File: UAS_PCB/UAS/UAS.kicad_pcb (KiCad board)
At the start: 2 copper layers, 50.8 x 47.6 mm, 17 parts, among them J1 SM02B-PASS-TBT, J2 SM02B-PASS-TBT, J3 SM02B-PASS-TBT, J4 SM02B-PASS-TBT, U1 JST-7-Pin, U10 UAS-rescue_7.5V-2.4A-Converte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, U11 JST-3-Pin, U12 Signal-Pad, U13 Signal-Pad, U2 5A-5V-Converter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

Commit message: slight adjustments to footprint placement
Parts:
- moved U9 0.32 mm to (159.0, 121.0)
- moved U10 0.10 mm to (155.4, 111.8)
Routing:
- net +7.5V: track 40.3 -> 38.6 mm
- net Net-(U13-Pad1): track 37.5 -> 36.9 mm
- net (no net): vias 0 -> 4
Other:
- outline, holes or cut-outs redrawn
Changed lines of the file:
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@@
   (general
     (thickness 1.6002)
-    (drawings 15227)
-    (tracks 197)
+    (drawings 15223)
+    (tracks 196)
     (zones 0)
     (modules 17)
@@
   )
   (setup
-    (last_trace_width 0.127)
+    (last_trace_width 0.6)
     (user_trace_width 0.15)
     (user_trace_width 0.2)
@@
     (user_via 0.9 0.4)
     (user_via 1.1 0.5)
+    (user_via 2.5 2)
     (uvia_size 0.6858)
     (uvia_drill 0.3302)
@@
   )
   (module UAS:Pololu_7.75V_2.4A_Step_Down_Regulator (layer Front)
-    (at 155.5 111.75 270)
+    (at 155.4 111.75 270)
     (fp_text reference U10 (at 0 4.25 180) (layer F.SilkS)
       (effects (font (size 1 1) (thickness 0.15)))
@@
   )
   (module "UAS:JST_SM03B-PASS-TBT(LF)(SN)" (layer Back)
-    (at 159.3215 121)
+    (at 159 121)
     (fp_text reference U9 (at 0 -3.75) (layer B.SilkS)
       (effects (font (size 1 1) (thickness 0.015)) (justify mirror))
@@
   (gr_line (start 152.542524 92.758045) (end 152.410237 92.542725) (layer B.SilkS) (width 0.0125))
   (gr_line (start 153.5 96) (end 153.514988 95.928529) (layer B.SilkS) (width 0.0125))
-  (gr_circle (center 120 118.545) (end 121 118.545) (layer Edge.Cuts) (width 0.1))
   (gr_line (start 168.26 118.544999) (end 168.26 76) (layer Edge.Cuts) (width 0.1))
   (gr_arc (start 120.000001 76) (end 120 73.46) (angle -90) (layer Edge.Cuts) (width 0.1))
@@
   (gr_line (start 165.72 73.46) (end 120 73.46) (layer Edge.Cuts) (width 0.1))
   (gr_line (start 120.000001 121.084999) (end 165.72 121.084999) (layer Edge.Cuts) (width 0.1))
-  (gr_circle (center 165.72 76) (end 166.72 76) (layer Edge.Cuts) (width 0.1))
-  (gr_circle (center 165.72 118.544999) (end 166.72 118.544999) (layer Edge.Cuts) (width 0.1))
   (gr_arc (start 165.72 118.544999) (end 165.72 121.084999) (angle -90) (layer Edge.Cuts) (width 0.1))
   (gr_line (start 117.460001 76) (end 117.460001 118.545) (layer Edge.Cuts) (width 0.1))
   (gr_arc (start 165.72 76) (end 168.26 76) (angle -90) (layer Edge.Cuts) (width 0.1))
-  (gr_circle (center 120 76) (end 121 76) (layer Edge.Cuts) (width 0.1))
+  (via (at 120 118.55) (size 2.5) (drill 2) (layers Front Back) (net 0) (status 40000))
+  (via (at 120 76) (size 2.5) (drill 2) (layers Front Back) (net 0) (status 40000))
+  (via (at 165.725 76) (size 2.5) (drill 2) (layers Front Back) (net 0) (status 40000))
+  (via (at 165.72 118.54) (size 2.5) (drill 2) (layers Front Back) (net 0) (status 40000))
   (via (at 151.77 99.85) (size 0.9) (drill 0.4) (layers Front Back) (net 1))
   (segment (start 151.77 91.88) (end 151.77 99.85) (width 0.6) (layer Back) (net 1))
@@
   (segment (start 125.25 118.72) (end 125.21 118.76) (width 0.6) (layer Front) (net 27))
   (segment (start 125.25 115.5) (end 125.25 118.72) (width 0.6) (layer Front) (net 27))
-  (segment (start 157.261533 112.009967) (end 157.3215 111.95) (width 0.4) (layer Back) (net 28))
   (via (at 131.3 120.457999) (size 0.9) (drill 0.4) (layers Front Back) (net 28))
   (segment (start 130.207999 120.457999) (end 128.5 118.75) (width 0.6) (layer Front) (net 28))
@@
   (segment (start 152.8 119.507989) (end 151.807989 120.5) (width 0.6) (layer Back) (net 28))
   (segment (start 152.8 118.4) (end 152.8 119.507989) (width 0.6) (layer Back) (net 28))
-  (segment (start 152.8 112.4) (end 153.65 111.7) (width 0.6) (layer Back) (net 28))
-  (segment (start 157.0715 111.7) (end 157.3215 111.95) (width 0.6) (layer Back) (net 28))
-  (segment (start 153.65 111.7) (end 157.0715 111.7) (width 0.6) (layer Back) (net 28))
   (via (at 152.8 118.4) (size 0.9) (drill 0.4) (layers Front Back) (net 28))
   (segment (start 152.8 112.4) (end 152.8 118.4) (width 0.6) (layer Front) (net 28))
   (via (at 152.8 112.4) (size 0.9) (drill 0.4) (layers Front Back) (net 28))
+  (segment (start 153.25 111.95) (end 152.8 112.4) (width 0.6) (layer Back) (net 28))
+  (segment (start 157 111.95) (end 153.25 111.95) (width 0.6) (layer Back) (net 28))
   (via (at 146.7 101.8) (size 1.1) (drill 0.5) (layers Front Back) (net 29))
   (via (at 137.8 74) (size 0.9) (drill 0.4) (layers Front Back) (net 29))
@@
   (segment (start 134.31 101.31) (end 133.5 100.5) (width 1) (layer Back) (net 30))
   (segment (start 143 118) (end 143 114.33) (width 0.6) (layer Front) (net 31))
-  (segment (start 147.88 109.46) (end 147.91 109.43) (width 0.6) (layer Front) (net 31))
   (segment (start 129.23 104.71) (end 129.23 104.08) (width 0.4) (layer Front) (net 31))
   (segment (start 126.5 107.44) (end 129.23 104.71) (width 0.6) (layer Front) (net 31))
@@
   (segment (start 143 110.87) (end 144.66 109.21) (width 0.6) (layer Front) (net 31))
   (segment (start 143 114.33) (end 143 111.12) (width 0.6) (layer Front) (net 31))
-  (segment (start 144.66 109.21) (end 147.88 109.21) (width 0.6) (layer Front) (net 31))
   (via (at 150.25 109.75) (size 0.9) (drill 0.4) (layers Front Back) (net 31))
   (segment (start 149.71 109.21) (end 150.25 109.75) (width 0.6) (layer Front) (net 31))
-  (segment (start 147.88 109.21) (end 149.71 109.21) (width 0.6) (layer Front) (net 31))
   (segment (start 151 109.75) (end 152.21 108.54) (width 0.6) (layer Back) (net 31))
   (segment (start 150.25 109.75) (end 151 109.75) (width 0.6) (layer Back) (net 31))
+  (segment (start 144.66 109.21) (end 147.78 109.21) (width 0.6) (layer Front) (net 31))
+  (segment (start 149.71 109.21) (end 147.78 109.21) (width 0.6) (layer Front) (net 31))
   (segment (start 126.75 111.95) (end 126.75 113.03) (width 0.4) (layer Back) (net 32))
   (segment (start 147.87 114.55) (end 147.88 114.54) (width 0.4) (layer Back) (net 32))
@@
   (segment (start 126.75 112.799962) (end 127.820038 113.87) (width 0.6) (layer Back) (net 32))
   (segment (start 126.75 111.95) (end 126.75 112.799962) (width 0.4) (layer Back) (net 32))
-  (segment (start 159.3215 113.0585) (end 159.3215 111.95) (width 0.4) (layer Back) (net 32))
   (segment (start 147.88 114.54) (end 148.54 113.88) (width 0.4) (layer Back) (net 32))
-  (segment (start 159.3215 112.388602) (end 159.3215 111.95) (width 0.4) (layer Back) (net 32))
   (segment (start 147.88 114.54) (end 148.44 113.98) (width 0.4) (layer Back) (net 32))
-  (segment (start 159.3215 112.9285) (end 159.3215 112.388602) (width 0.6) (layer Back) (net 32))
   (segment (start 132.85 114.29) (end 132.43 113.87) (width 0.6) (layer Back) (net 32))
-  (segment (start 147.88 114.29) (end 132.85 114.29) (width 0.6) (layer Back) (net 32))
   (segment (start 148.27 113.9) (end 147.88 114.29) (width 0.6) (layer Back) (net 32))
-  (segment (start 157.990102 113.9) (end 148.27 113.9) (width 0.6) (layer Back) (net 32))
-  (segment (start 159.3215 112.568602) (end 157.990102 113.9) (width 0.6) (layer Back) (net 32))
-  (segment (start 159.3215 111.95) (end 159.3215 112.568602) (width 0.6) (layer Back) (net 32))
+  (segment (start 132.85 114.29) (end 147.78 114.29) (width 0.6) (layer Back) (net 32))
+  (segment (start 148.17 113.9) (end 147.78 114.29) (width 0.6) (layer Back) (net 32))
+  (segment (start 157.990102 113.9) (end 148.17 113.9) (width 0.6) (layer Back) (net 32))
+  (segment (start 159 112.890102) (end 157.990102 113.9) (width 0.6) (layer Back) (net 32))
+  (segment (start 159 111.95) (end 159 112.890102) (width 0.6) (layer Back) (net 32))
 )

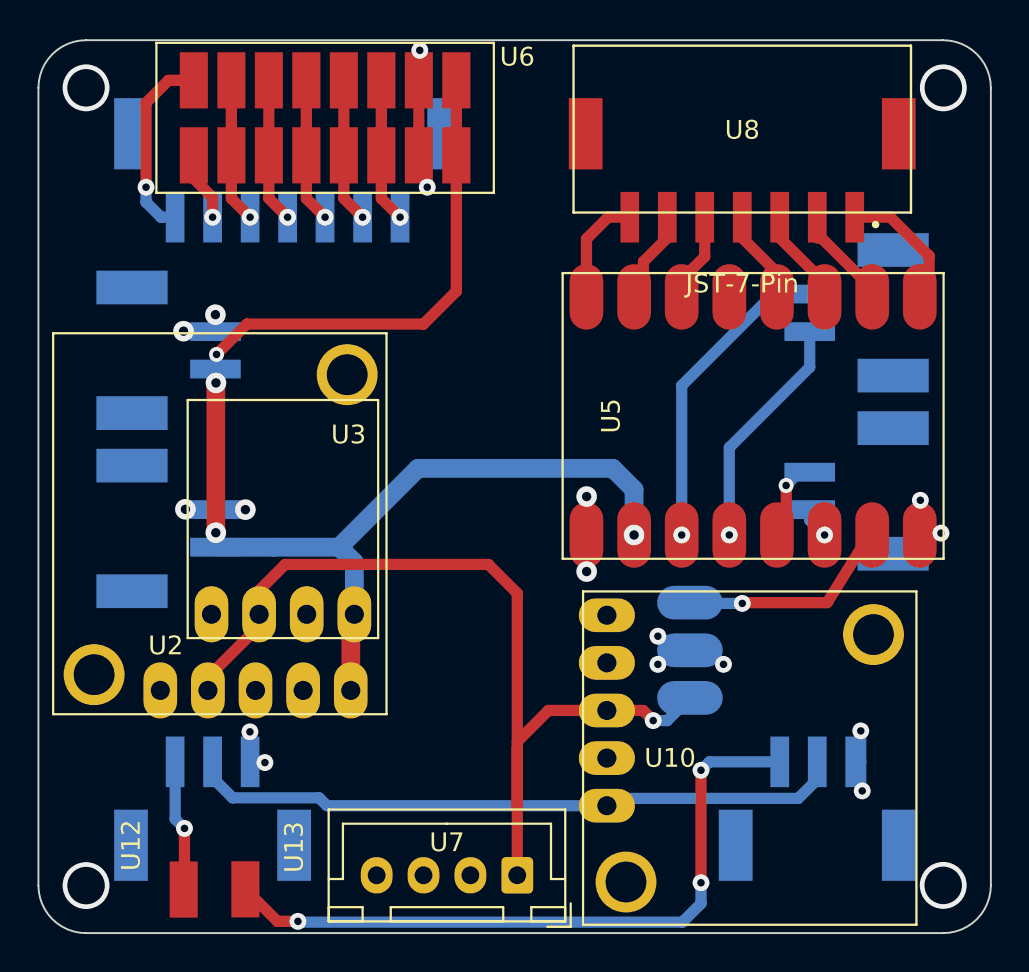
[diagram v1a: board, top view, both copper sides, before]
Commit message: added LeMonke Graphics, still needs trace width adjustments
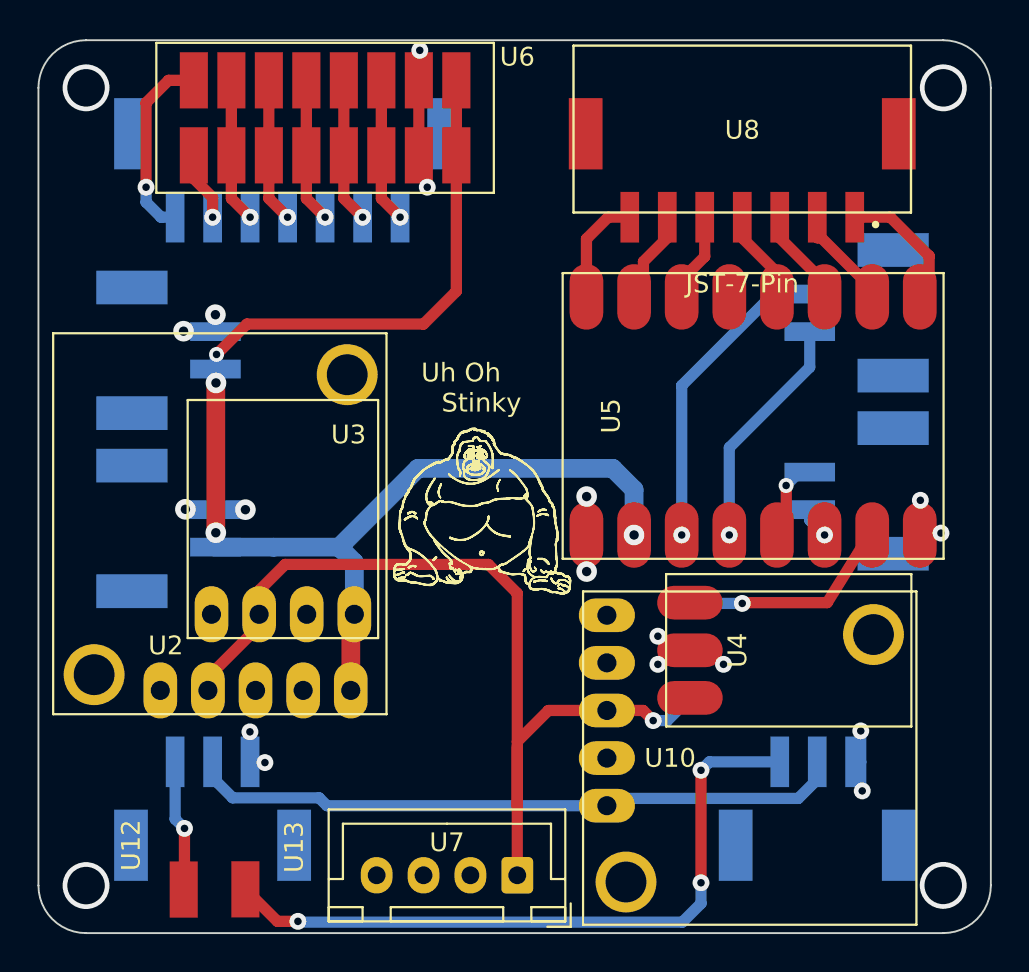
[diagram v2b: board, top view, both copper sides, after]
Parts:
- U4: moved to F.Cu
- turned U4 to 270 degrees
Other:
- board text added: "Uh Oh Stinky"

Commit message: trace width changes
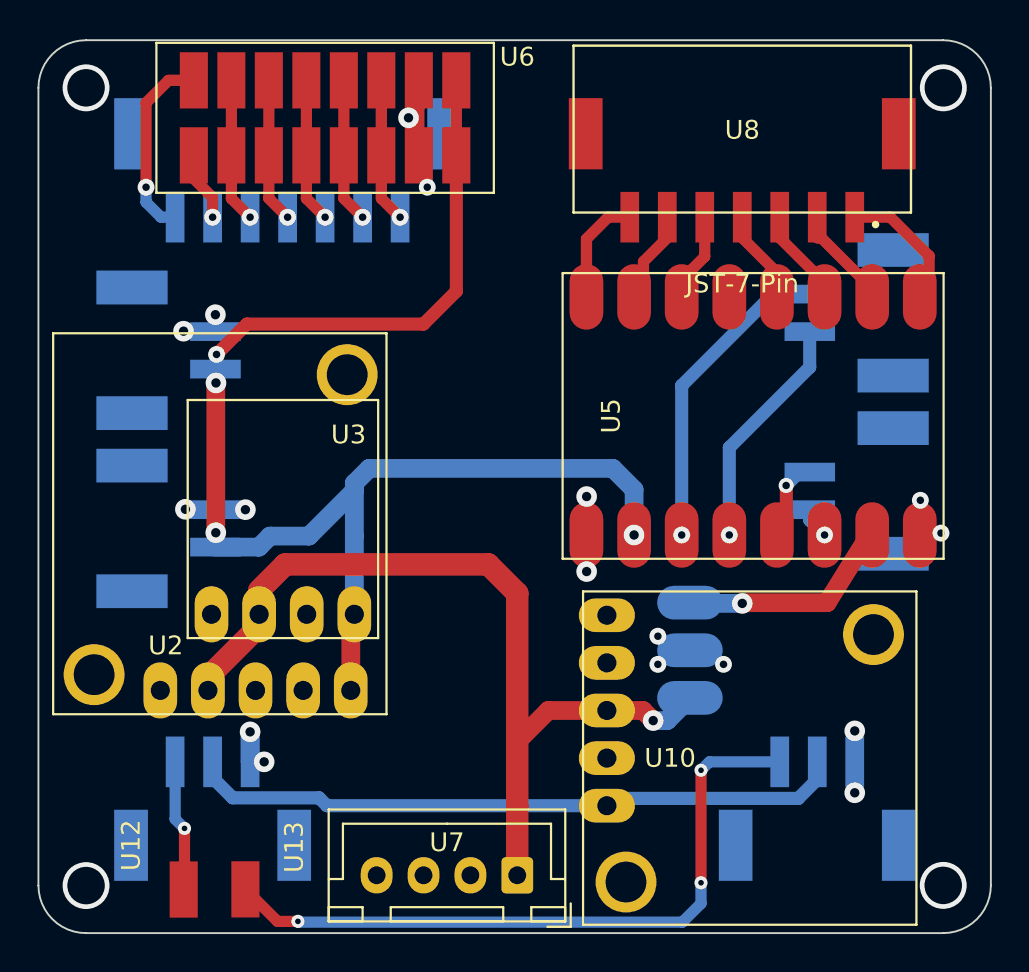
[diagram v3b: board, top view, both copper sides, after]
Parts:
- U4: moved to B.Cu
- turned U4 to 90 degrees
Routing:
- net +5V: track 72.7 -> 76.0 mm
- net GND: track 12.6 -> 14.9 mm

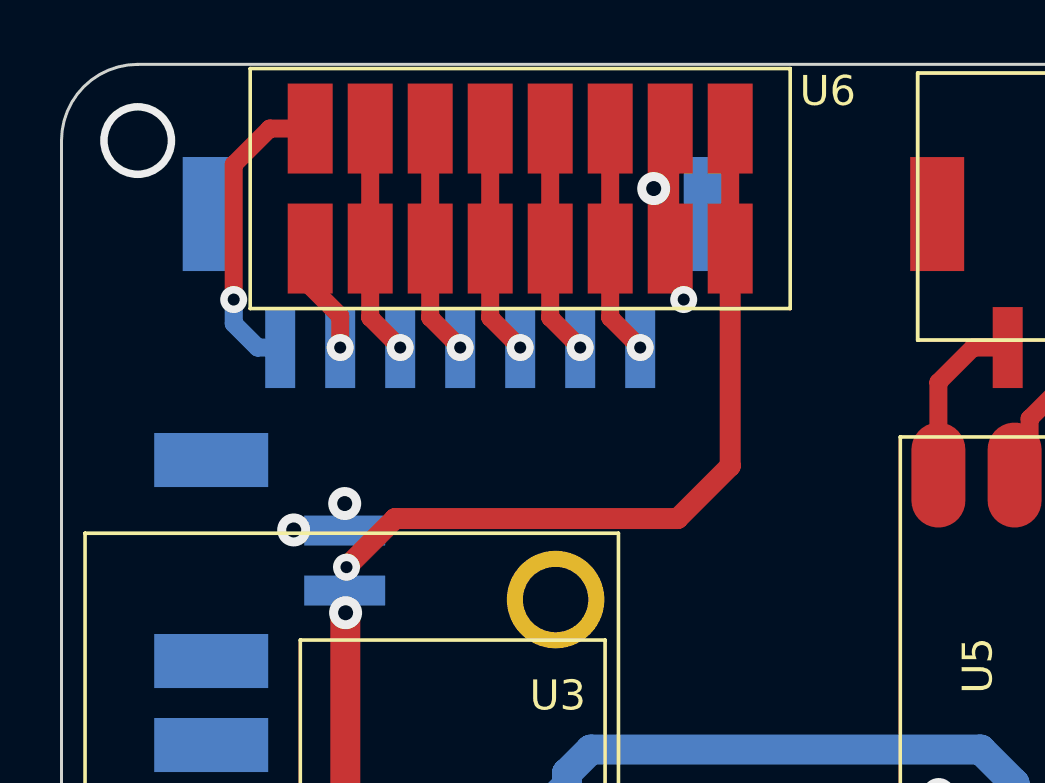
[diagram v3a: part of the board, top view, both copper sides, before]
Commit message: flipped PCS connector to front
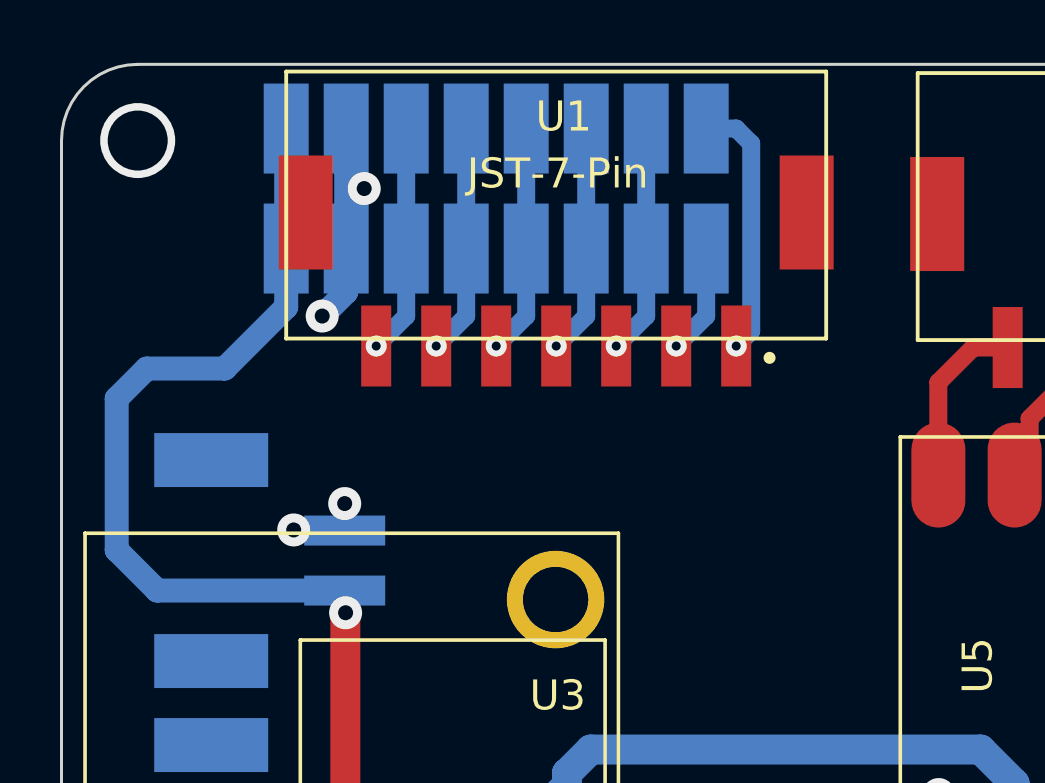
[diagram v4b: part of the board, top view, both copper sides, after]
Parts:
- U1: moved to F.Cu
- U6: moved to B.Cu
- moved U1 3.20 mm to (133.9, 73.7), turned to 0 degrees
- moved U6 0.80 mm to (131.9, 79.6), turned to 180 degrees
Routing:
- net GND: track 14.9 -> 17.5 mm
- net Net-(U1-Pad1): track 10.2 -> 8.66 mm
- net +5V: track 76.0 -> 75.8 mm, vias 4 -> 3

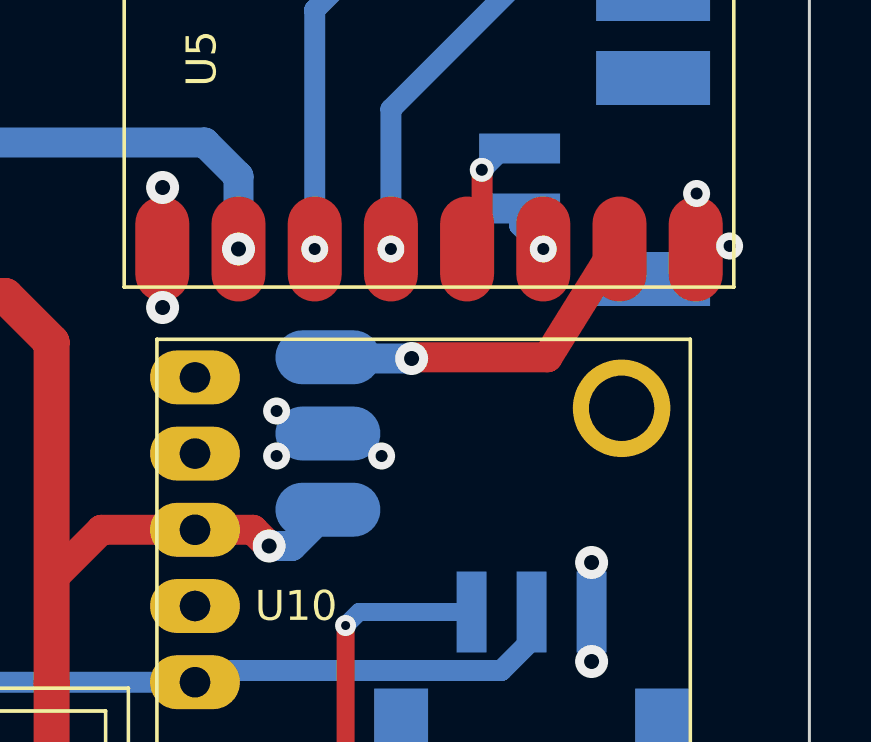
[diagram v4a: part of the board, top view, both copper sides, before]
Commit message: 12v step up was backwards
should double check other pinouts as well
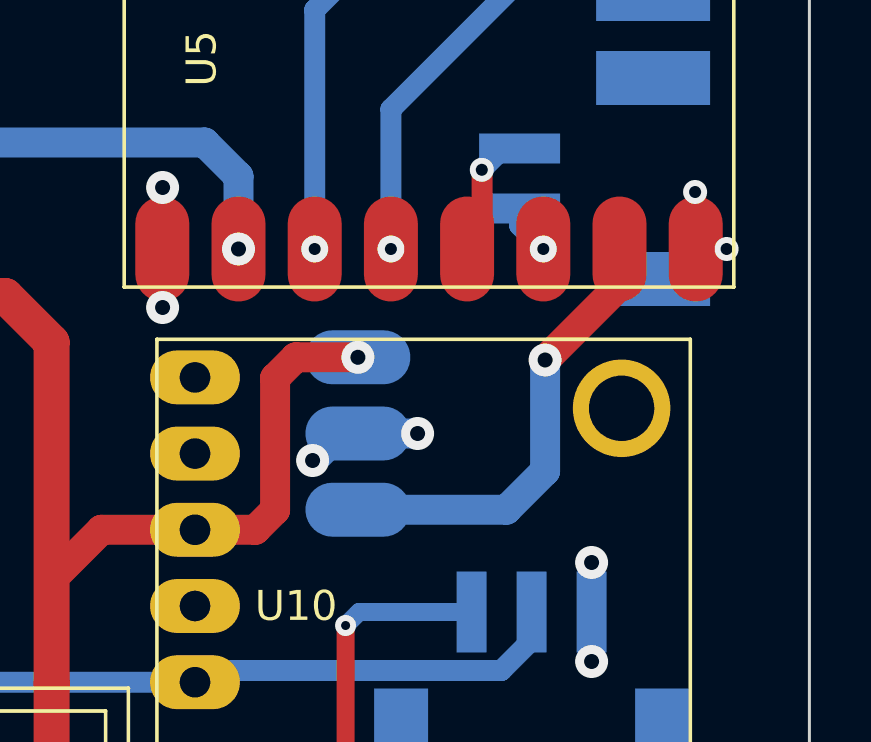
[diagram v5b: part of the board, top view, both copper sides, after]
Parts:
- moved U4 1.00 mm to (155.8, 106.0)
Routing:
- net GND: track 17.5 -> 24.3 mm, vias 17 -> 16
- net +12V: track 50.3 -> 55.6 mm
- net Net-(U4-Pad3): track 12.4 -> 15.7 mm
